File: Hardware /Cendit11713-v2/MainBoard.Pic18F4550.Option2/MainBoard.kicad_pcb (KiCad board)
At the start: 2 copper layers, 52 parts, among them CON1 POWER_CON, CON2 ICSP_CON, CON3 USB_CON, J1 RESET_CON, J2 PIN_HEADER_20P, J3 PIN_HEADER_20P, P1 SATA_PLUG _22P_SMT, P2 SATA_PLUG _22P_SMT, U1 PIC18F4550-I/P, U2 MPL3115A2, U3 PCF85263A, Y1 Crystal, Y2 32.768KHZ

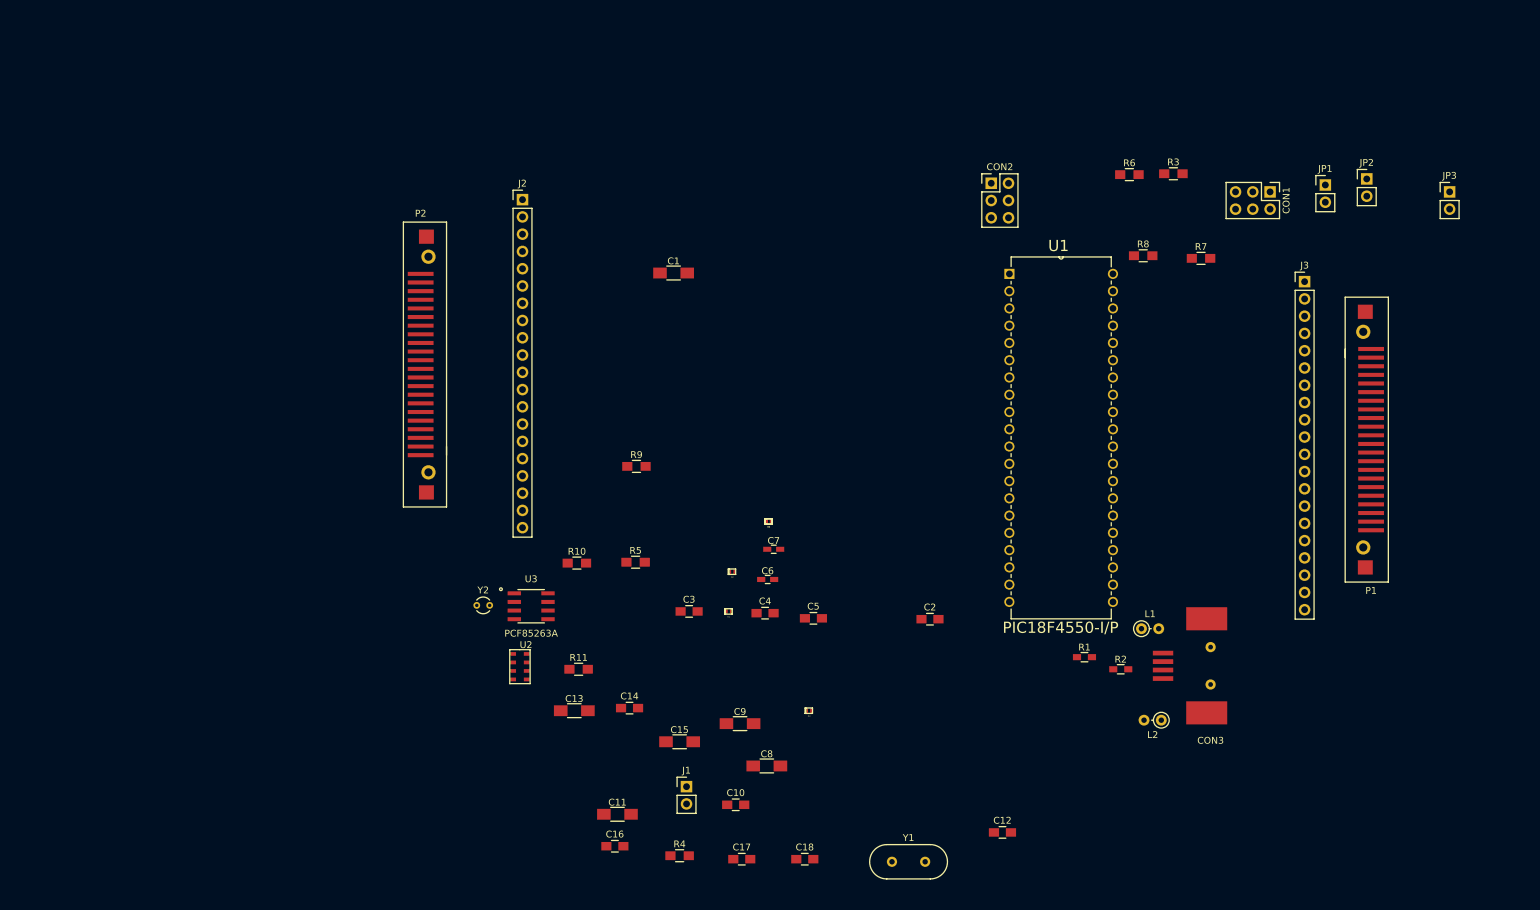
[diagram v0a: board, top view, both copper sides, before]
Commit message: En CenditLab.Reducido + Cendit11713
  - Hardware tarjeta madre opcion 2, esquematico + PCB
  - Software UI vistas de setup + steps
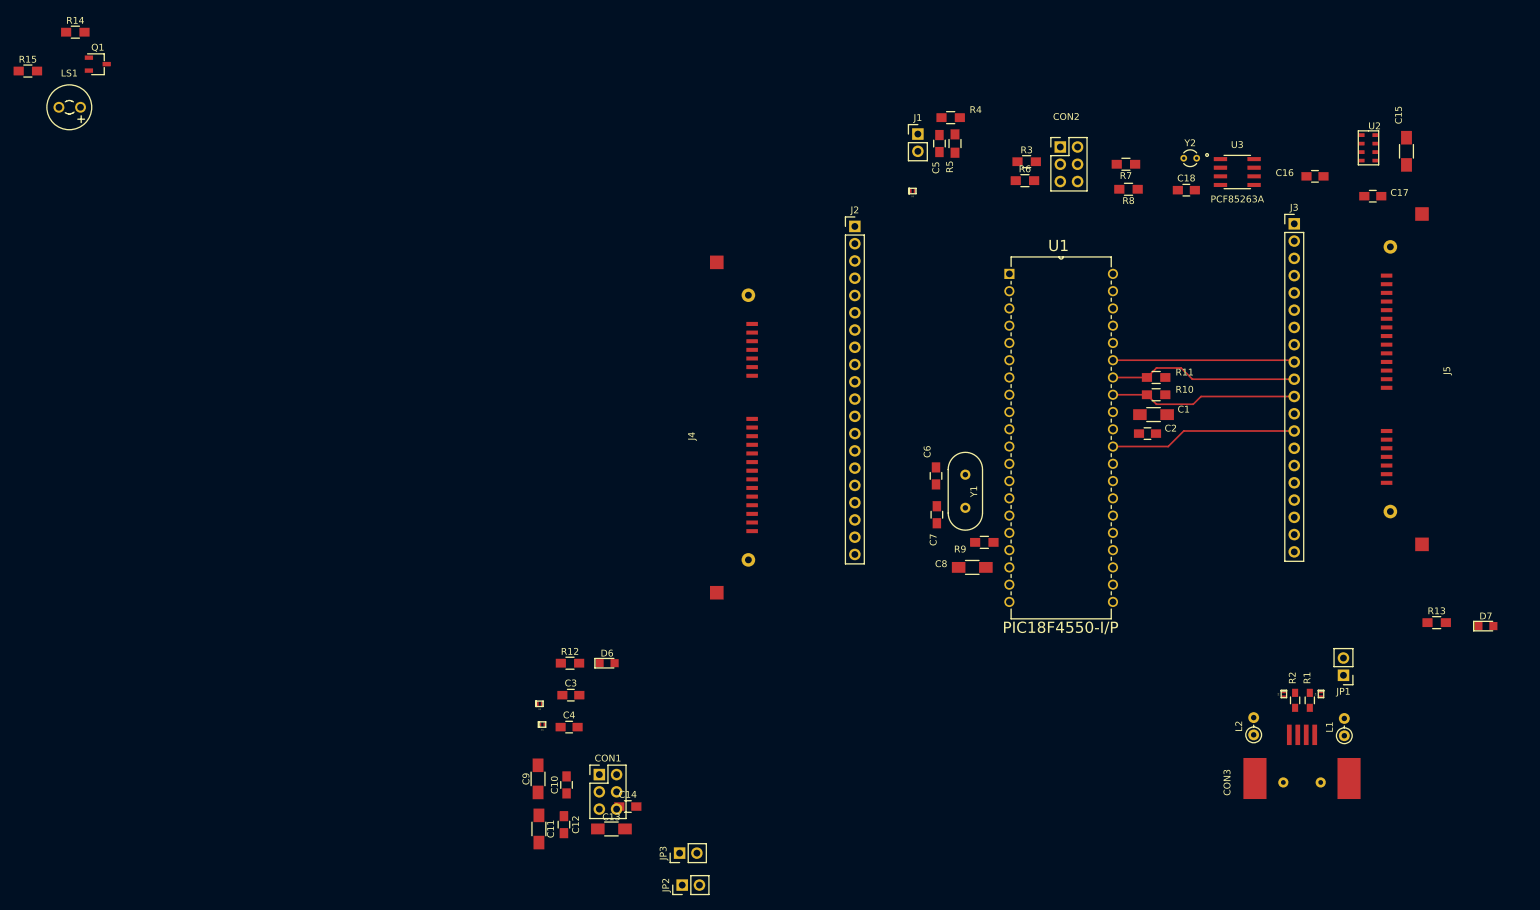
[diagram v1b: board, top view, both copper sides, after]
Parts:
- removed P1, P2: SATA_PLUG _22P_SMT, CenditFootprints:SATA_BACKPLANE_RECEPTACLE_VERTICAL_22P
- added D6: LED, LEDs:LED_0805, F.Cu at (124.7, 125.9)
- added D7: LED, LEDs:LED_0805, F.Cu at (254.0, 120.4)
- added J4: SATA_PLUG _22P_SMT, CenditFootprints:SATA_PLUG_22P_SMT, F.Cu at (146.1, 75.9)
- added J5: SATA_PLUG _22P_SMT, CenditFootprints:SATA_PLUG_22P_SMT, F.Cu at (239.4, 99.3)
- added LS1: Speaker_Crystal, Buzzers_Beepers:MagneticBuzzer_Kingstate_KCG0601, F.Cu at (44.1, 44.1)
- added Q1: 2N2222, TO_SOT_Packages_SMD:TSOT-23, F.Cu at (49.8, 37.7)
- added R12: 300, Resistors_SMD:R_0805_HandSoldering, F.Cu at (119.3, 125.9)
- added R13: 300, Resistors_SMD:R_0805_HandSoldering, F.Cu at (246.8, 119.9)
- added R14: 300, Resistors_SMD:R_0805_HandSoldering, F.Cu at (46.5, 33.0)
- added R15: 1k, Resistors_SMD:R_0805_HandSoldering, F.Cu at (39.5, 38.7)
- C6, C7: footprint Capacitors_SMD:C_0603_HandSoldering -> Capacitors_SMD:C_0805_HandSoldering
- D1, D2: value D_Schottky -> SP1003-01ETG
- moved JP3 149.3 mm to (135.4, 153.8), turned to 90 degrees
- moved U2 146.3 mm to (236.7, 50.0)
- moved JP2 144.7 mm to (135.8, 158.5), turned to 90 degrees
- moved C16 142.6 mm to (228.9, 54.2)
- moved C15 137.8 mm to (242.3, 50.5), turned to 270 degrees
- moved C17 134.7 mm to (237.4, 57.1)
- moved CON1 130.7 mm to (123.6, 142.2), turned to 0 degrees
- moved Y2 123.1 mm to (209.6, 51.6)
- moved U3 122.0 mm to (217.4, 53.6)
- moved R4 115.7 mm to (175.3, 45.6), turned to 180 degrees
- moved C18 113.3 mm to (209.9, 56.3)
- moved J1 101.9 mm to (170.4, 48.0)
- moved R11 95.2 mm to (205.5, 83.8), turned to 180 degrees
- moved R10 88.7 mm to (205.5, 86.4), turned to 180 degrees
- moved D4 85.1 mm to (229.7, 130.4), turned to 270 degrees
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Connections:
- C15 pad 1: Net-(C15-Pad1) -> /VDD_3V
- C16 pad 1: Net-(C15-Pad1) -> /VDD_3V
- C18 pad 1: Net-(C18-Pad1) -> /VDD_3V
- D3 pad 1: Net-(D3-Pad1) -> /USB_D+
- J2 pad 1: Net-(J2-Pad1) -> /VPWR
- J2 pad 2: Net-(J2-Pad2) -> GNDPWR
- J2 pad 3: Net-(J2-Pad3) -> /VCC_5V
- J2 pad 4: Net-(J2-Pad4) -> /VCC_3V
- J2 pad 5: Net-(J2-Pad5) -> GNDD
- J3 pad 1: Net-(J3-Pad1) -> /VPWR
- J3 pad 2: Net-(J3-Pad2) -> /GND_PWR
- J3 pad 3: Net-(J3-Pad3) -> /VCC_5V
- J3 pad 4: Net-(J3-Pad4) -> /VCC_3V
- R4 pad 1: VCC -> VDD
- U2 pad 1: Net-(C15-Pad1) -> /VDD_3V
- U2 pad 4: Net-(C15-Pad1) -> /VDD_3V
- U3 pad 8: Net-(C18-Pad1) -> /VDD_3V
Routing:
- net /PB1: track 0.00 -> 27.9 mm
- net /PB0: track 0.00 -> 27.7 mm
- net //CS_VIKING: track 0.00 -> 27.6 mm
- net /PB2: track 0.00 -> 26.8 mm

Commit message: En Cendit11713 diseño de MainBoard Option 2
  - Edicion esquematico +diseño PCB + diseño de fuente
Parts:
- CON1: value POWER_CON -> POWER_BUS; footprint Pin_Headers:Pin_Header_Straight_2x03_Pitch2.54mm -> Pin_Headers:Pin_Header_Straight_2x05
- CON2: footprint Pin_Headers:Pin_Header_Straight_2x03_Pitch2.54mm -> Pin_Headers:Pin_Header_Straight_2x03
- moved C15 64.6 mm to (209.3, 106.0)
- moved U2 60.3 mm to (216.0, 106.6)
- moved C16 57.3 mm to (206.6, 107.0), turned to 270 degrees
- moved C17 55.7 mm to (212.3, 106.9), turned to 270 degrees
- moved C11 30.8 mm to (145.4, 149.0)
- moved C13 30.2 mm to (149.6, 132.3), turned to 270 degrees
- moved C14 29.8 mm to (153.2, 131.3), turned to 270 degrees
- moved JP2 29.1 mm to (154.9, 136.7), turned to 270 degrees
- moved CON1 26.4 mm to (144.8, 126.5), turned to 90 degrees
- moved L2 21.9 mm to (200.7, 125.7)
- moved D3 18.6 mm to (209.3, 119.4)
- moved R1 18.1 mm to (213.6, 120.4)
- moved R2 18.1 mm to (211.5, 120.4)
- moved CON3 18.1 mm to (212.3, 125.7)
- moved C12 18.0 mm to (101.6, 156.2)
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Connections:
- net /VDD_MAIN renamed Net-(D2-Pad2)
- CON1 pad 6: GNDA -> GNDD
- J4 pad 1: /PA0 -> (no net)
- J4 pad 10: /PE2 -> /PA3
- J4 pad 11: /PC0 -> /PA4
- J4 pad 12: /PC1 -> /PA5
- J4 pad 13: /PC2 -> GNDD
- J4 pad 14: /PD0 -> /PE0
- J4 pad 15: /PD1 -> /PE1
- J4 pad 16: Net-(J4-Pad16) -> /PE2
- J4 pad 17: GNDD -> /PC0
- J4 pad 18: /VCC_3V -> /PC1
- J4 pad 19: /VCC_5V -> /PC2
- J4 pad 2: /PA1 -> /VPWR
- J4 pad 20: GNDPWR -> /PD0
- J4 pad 21: /VPWR -> /PD1
- J4 pad 3: /PA2 -> GNDPWR
- J4 pad 4: /PA3 -> /VCC_5V
- J4 pad 5: /PA4 -> /VCC_3V
- J4 pad 6: /PA5 -> GNDD
- J4 pad 7: GNDD -> /PA0
- J4 pad 8: /PE0 -> /PA1
- J4 pad 9: /PE1 -> /PA2
- R6 pad 2: Net-(CON2-Pad5) -> Net-(CON2-Pad6)
- R8 pad 2: Net-(CON2-Pad6) -> Net-(CON2-Pad5)
- U2 pad 5: Net-(U2-Pad5) -> (no net)
- U2 pad 6: Net-(U2-Pad6) -> (no net)
- U3 pad 3: Net-(BT1-Pad1) -> (no net)
- U3 pad 7: Net-(U3-Pad7) -> (no net)
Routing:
- net /PB6: track 0.00 -> 67.7 mm
- net /PB7: track 0.00 -> 63.7 mm
- net /MISO: track 0.00 -> 56.6 mm
- net /MOSI: track 0.00 -> 52.5 mm
- net //RST_KEY: track 0.00 -> 50.2 mm
- net //RST_LAN: track 0.00 -> 50.1 mm
- net //RST_GPIB: track 0.00 -> 48.0 mm
- net /PB4: track 0.00 -> 47.3 mm
- net /PB3: track 0.00 -> 47.0 mm
- net //RST_VIKING: track 0.00 -> 45.8 mm
- net //CS_LAN: track 0.00 -> 44.0 mm
- net /USB_D+: track 0.00 -> 41.9 mm
- net /USB_D-: track 0.00 -> 41.1 mm
- net GNDD: track 0.00 -> 38.0 mm, vias 0 -> 3
- net /PE2: track 0.00 -> 33.3 mm
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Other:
- net class DATA added: clearance 0.25, trace_width 0.5, via_dia 0.6, via_drill 0.4
- net class GND added: clearance 0.25, trace_width 0.8, via_dia 1.5, via_drill 0.4
- net class GNDD added: clearance 0.25, trace_width 0.8, via_dia 1.5, via_drill 0.4
- net class GNDPWR added: clearance 0.5, trace_width 0.8, via_dia 0.6, via_drill 0.4
- net class OSC added: clearance 0.25, trace_width 0.35, via_dia 0.6, via_drill 0.4
- net class USB_PAIR added: clearance 0.2, trace_width 0.35, via_dia 0.6, via_drill 0.4
- net class VDD added: clearance 0.3, trace_width 0.6, via_dia 1.5, via_drill 0.4
- net class VPWR added: clearance 0.3, trace_width 0.8, via_dia 0.6, via_drill 0.4

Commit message: En CenditLab + Cendit11713
  - Software trabajo en clases UI + fxml
  - Hardware diseño de tarjeta madre opcion 2
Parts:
- removed J3: PIN_HEADER_20P, Pin_Headers:Pin_Header_Straight_1x20_Pitch2.54mm
- removed J5: SATA_PLUG _22P_SMT, CenditFootprints:SATA_PLUG_22P_SMT
- removed JP3: JMP3V, Pin_Headers:Pin_Header_Straight_1x02_Pitch2.54mm
- added P1: DEBUG_HEADER_21P, CenditFootprints2:DEBUG_PIN_HEADER_21P, F.Cu at (161.9, 67.4)
- added P2: DEBUG_HEADER_21P, CenditFootprints2:DEBUG_PIN_HEADER_21P, F.Cu at (222.6, 67.8)
- added R16: RP, Resistors_SMD:R_0603_HandSoldering, F.Cu at (175.9, 86.6)
- added R17: RP, Resistors_SMD:R_0603_HandSoldering, F.Cu at (175.9, 89.2)
- added R18: RP, Resistors_SMD:R_0603_HandSoldering, F.Cu at (176.0, 91.7)
- added R19: RP, Resistors_SMD:R_0603_HandSoldering, F.Cu at (175.9, 71.4)
- added R20: RP, Resistors_SMD:R_0603_HandSoldering, F.Cu at (175.9, 73.9)
- added R21: RP, Resistors_SMD:R_0603_HandSoldering, F.Cu at (175.9, 76.5)
- added R22: RP, Resistors_SMD:R_0603_HandSoldering, F.Cu at (176.1, 106.0)
- added R23: RP, Resistors_SMD:R_0603_HandSoldering, F.Cu at (175.9, 79.0)
- added R24: RP, Resistors_SMD:R_0603_HandSoldering, F.Cu at (176.1, 108.2)
- added R25: RP, Resistors_SMD:R_0603_HandSoldering, F.Cu at (175.9, 81.5)
- added R26: RP, Resistors_SMD:R_0603_HandSoldering, F.Cu at (176.3, 110.4)
- added R27: RP, Resistors_SMD:R_0603_HandSoldering, F.Cu at (175.9, 84.1)
- added R28: RP, Resistors_SMD:R_0603_HandSoldering, F.Cu at (204.7, 106.9)
- added R29: RP, Resistors_SMD:R_0603_HandSoldering, F.Cu at (204.9, 86.6)
- added R30: RP, Resistors_SMD:R_0603_HandSoldering, F.Cu at (204.7, 104.4)
- added R31: RP, Resistors_SMD:R_0603_HandSoldering, F.Cu at (204.9, 84.1)
- added R32: RP, Resistors_SMD:R_0603_HandSoldering, F.Cu at (204.9, 81.5)
- added R33: RP, Resistors_SMD:R_0603_HandSoldering, F.Cu at (176.3, 115.3)
- added R34: RP, Resistors_SMD:R_0603_HandSoldering, F.Cu at (204.9, 79.0)
- added R35: RP, Resistors_SMD:R_0603_HandSoldering, F.Cu at (176.3, 117.5)
- added R36: RP, Resistors_SMD:R_0603_HandSoldering, F.Cu at (204.9, 76.5)
- added R37: RP, Resistors_SMD:R_0603_HandSoldering, F.Cu at (205.9, 111.6)
- added R38: RP, Resistors_SMD:R_0603_HandSoldering, F.Cu at (204.9, 73.9)
- added R39: RP, Resistors_SMD:R_0603_HandSoldering, F.Cu at (205.9, 109.3)
- added R40: RP, Resistors_SMD:R_0603_HandSoldering, F.Cu at (205.0, 71.4)
- added R41: RP, Resistors_SMD:R_0603_HandSoldering, F.Cu at (204.6, 101.9)
- added R42: RP, Resistors_SMD:R_0603_HandSoldering, F.Cu at (205.0, 68.8)
- added R43: RP, Resistors_SMD:R_0603_HandSoldering, F.Cu at (204.7, 99.3)
- added R44: RP, Resistors_SMD:R_0603_HandSoldering, F.Cu at (204.7, 96.8)
- added R45: RP, Resistors_SMD:R_0603_HandSoldering, F.Cu at (204.7, 94.2)
- added R46: 0, Resistors_SMD:R_0805_HandSoldering, F.Cu at (178.6, 133.2)
- CON3: footprint CenditFootprints:USB_SMT_B -> CenditFootprints2:USB_SMT_B
- D1, D2, D3, D4, D5: footprint CenditFootprints:SP1003-01ETG -> CenditFootprints2:SP1003-01ETG
- J2: value PIN_HEADER_20P -> SATA_PLUG _22P_SMT; footprint Pin_Headers:Pin_Header_Straight_1x20_Pitch2.54mm -> CenditFootprints2:SATA_PLUG_22P_SMT
- J4: footprint CenditFootprints:SATA_PLUG_22P_SMT -> CenditFootprints2:SATA_PLUG_22P_SMT
- JP2: value JMP5V -> JMP_3V_5V; footprint Pin_Headers:Pin_Header_Straight_1x02_Pitch2.54mm -> Pin_Headers:Pin_Header_Straight_1x03
- R8: value 1.5K -> 100
- U1: footprint PIC18F4550-I_P:DIP254P1524X635-40 -> CenditFootprints2:PIC18F4550-PDIP
- U2: footprint CenditFootprints:MPL3115A2 -> CenditFootprints2:MPL3115A2
- U3: footprint CenditFootprints:PCF85263A_SO8 -> CenditFootprints2:PCF85263A_SO8
- moved R15 120.8 mm to (158.1, 61.5)
- moved Q1 117.1 mm to (164.7, 60.3)
- moved R14 114.4 mm to (158.2, 57.3), turned to 180 degrees
- moved LS1 106.1 mm to (149.1, 59.1)
- moved J2 80.9 mm to (233.2, 105.9), turned to 90 degrees
- moved D7 80.8 mm to (210.3, 58.8), turned to 270 degrees
- moved R13 72.2 mm to (210.3, 64.0), turned to 90 degrees
- moved R12 67.8 mm to (200.3, 124.5)
- moved C4 64.3 mm to (196.1, 126.1), turned to 270 degrees
- moved C12 62.6 mm to (157.7, 128.5)
- moved D2 62.3 mm to (190.0, 124.6), turned to 180 degrees
- moved D6 62.1 mm to (200.0, 126.7), turned to 180 degrees
- moved D1 62.1 mm to (190.0, 125.9), turned to 180 degrees
- moved C3 61.2 mm to (193.7, 126.1), turned to 270 degrees
- moved C9 60.4 mm to (154.8, 129.5), turned to 270 degrees
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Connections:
- C6 pad 2: GND -> GNDD
- C7 pad 2: GND -> GNDD
- CON3 pad 2: Net-(CON3-Pad2) -> /D-
- CON3 pad 3: Net-(CON3-Pad3) -> /D+
- D3 pad 1: /USB_D+ -> /D+
- D4 pad 1: /USB_D- -> /D-
- D5 pad 2: GNDD -> (no net)
- J2 pad 1: /VPWR -> //RST_KEY
- J2 pad 10: /PA4 -> /PB0
- J2 pad 11: /PA5 -> /PB1
- J2 pad 12: GNDD -> /PB2
- J2 pad 13: /PE0 -> /PB3
- J2 pad 14: /PE1 -> /PB4
- J2 pad 15: /PE2 -> /PB6
- J2 pad 16: /PC0 -> /PB7
- J2 pad 17: /PC1 -> GNDD
- J2 pad 18: /PC2 -> /VCC_3V
- J2 pad 19: /PD0 -> /VCC_5V
- J2 pad 2: GNDPWR -> //RST_GPIB
- J2 pad 20: /PD1 -> /GND_PWR
- J2 pad 3: /VCC_5V -> /MISO
- J2 pad 4: /VCC_3V -> /MOSI
- J2 pad 5: GNDD -> //RST_LAN
- J2 pad 6: /PA0 -> //RST_VIKING
- J2 pad 7: /PA1 -> //CS_LAN
- J2 pad 8: /PA2 -> //CS_VIKING
- J2 pad 9: /PA3 -> GNDD
- J4 pad 13: GNDD -> /PE0
- J4 pad 14: /PE0 -> /PE1
- J4 pad 15: /PE1 -> /PE2
- J4 pad 16: /PE2 -> GNDD
- R1 pad 2: Net-(CON3-Pad2) -> /D-
- R2 pad 2: Net-(CON3-Pad3) -> /D+
- R3 pad 1: /PB7 -> /PGD
- R7 pad 1: /PB6 -> /PGC
- U1 pad 10: /PE2 -> /RE2
- U1 pad 15: /PC0 -> /RC0
- U1 pad 16: /PC1 -> /RC1
- U1 pad 17: /PC2 -> /RC2
- U1 pad 19: /PD0 -> /RD0
- U1 pad 2: /PA0 -> /RA0
- U1 pad 20: /PD1 -> /RD1
- U1 pad 21: //RST_KEY -> /RD2
- U1 pad 22: //RST_GPIB -> /RD3
- U1 pad 25: /MISO -> /RC6
- U1 pad 26: /MOSI -> /RC7
- U1 pad 27: //RST_LAN -> /RD4
- U1 pad 28: //RST_VIKING -> /RD5
- U1 pad 29: //CS_LAN -> /RD6
- U1 pad 3: /PA1 -> /RA1
- U1 pad 30: //CS_VIKING -> /RD7
- U1 pad 33: /PB0 -> /RB0
- U1 pad 34: /PB1 -> /RB1
- U1 pad 35: /PB2 -> /RB2
- U1 pad 36: /PB3 -> /RB3
- U1 pad 37: /PB4 -> /RB4
- U1 pad 39: /PB6 -> /PGC
- U1 pad 4: /PA2 -> /RA2
- U1 pad 40: /PB7 -> /PGD
- U1 pad 5: /PA3 -> /RA3
- U1 pad 6: /PA4 -> /RA4
- U1 pad 7: /PA5 -> /RA5
- U1 pad 8: /PE0 -> /RE0
- U1 pad 9: /PE1 -> /RE1
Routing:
- net GNDD: track 38.0 -> 177.3 mm, vias 3 -> 5
- net GNDPWR: track 0.00 -> 52.0 mm
- net /VPWR: track 20.7 -> 67.4 mm, vias 0 -> 1
- net /PB6: track 67.7 -> 33.6 mm
- net /VCC_5V: track 20.0 -> 52.8 mm, vias 0 -> 1
- net /PB7: track 63.7 -> 35.2 mm
- net /PGC: track 0.00 -> 25.8 mm
- net /PB0: track 54.8 -> 34.4 mm
- net /PB1: track 56.2 -> 37.8 mm
- net /MISO: track 56.6 -> 38.4 mm
- net /PGD: track 0.00 -> 17.7 mm
- net /MOSI: track 52.5 -> 35.1 mm
- net /PB4: track 47.3 -> 30.5 mm
- net /VDD_3V: track 0.00 -> 16.3 mm, vias 0 -> 1
- net /MCLR_INT: track 0.00 -> 15.8 mm
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- added copper zone on F.Cu, net GNDD
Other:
- net class DATA: trace_width 0.5 -> 0.635
- net class Default: clearance 0.2 -> 0.25; trace_width 0.25 -> 0.635; via_dia 0.6 -> 1.5
- net class OSC: trace_width 0.35 -> 0.5
- net class USB_PAIR: clearance 0.2 -> 0.25; trace_width 0.35 -> 0.25
- net class VDD: via_dia 1.5 -> 1.6
- net class VPWR: via_dia 0.6 -> 1.6
- rule trace_clearance: 0.2 -> 0.25
